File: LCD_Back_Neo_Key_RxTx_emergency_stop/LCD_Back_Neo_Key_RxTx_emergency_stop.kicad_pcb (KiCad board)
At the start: 2 copper layers, 109.7 x 102.1 mm, 27 parts, among them J1 Screw_Terminal_01x14, J2 Conn_01x20_Female, J3 Conn_01x08_Male_KeyPad, J4 Display_support_pin, J5 Display_support_pin, K1 FINDER-34.51, K2 FINDER-34.51, K3 FINDER-34.51, K4 FINDER-34.51, Q1 BC337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

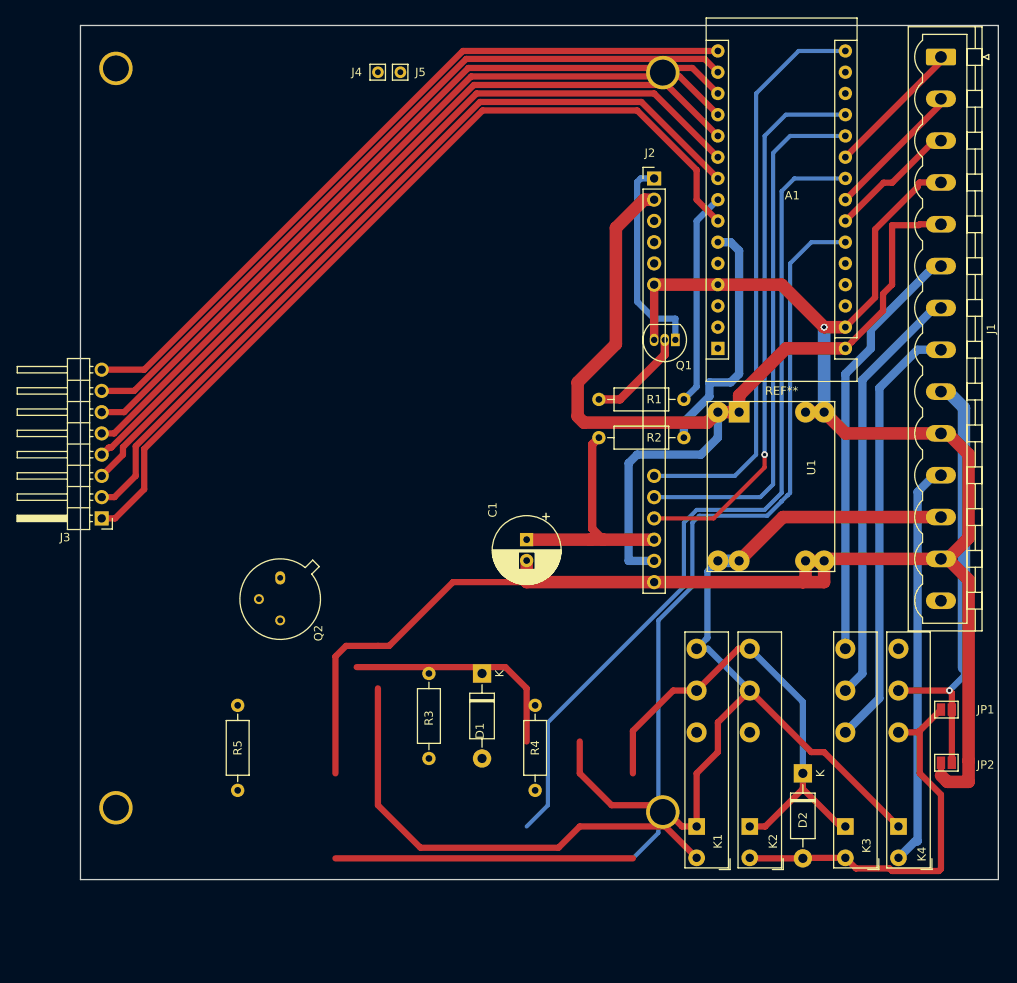
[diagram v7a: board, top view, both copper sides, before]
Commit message: make mounting holes free from tracks
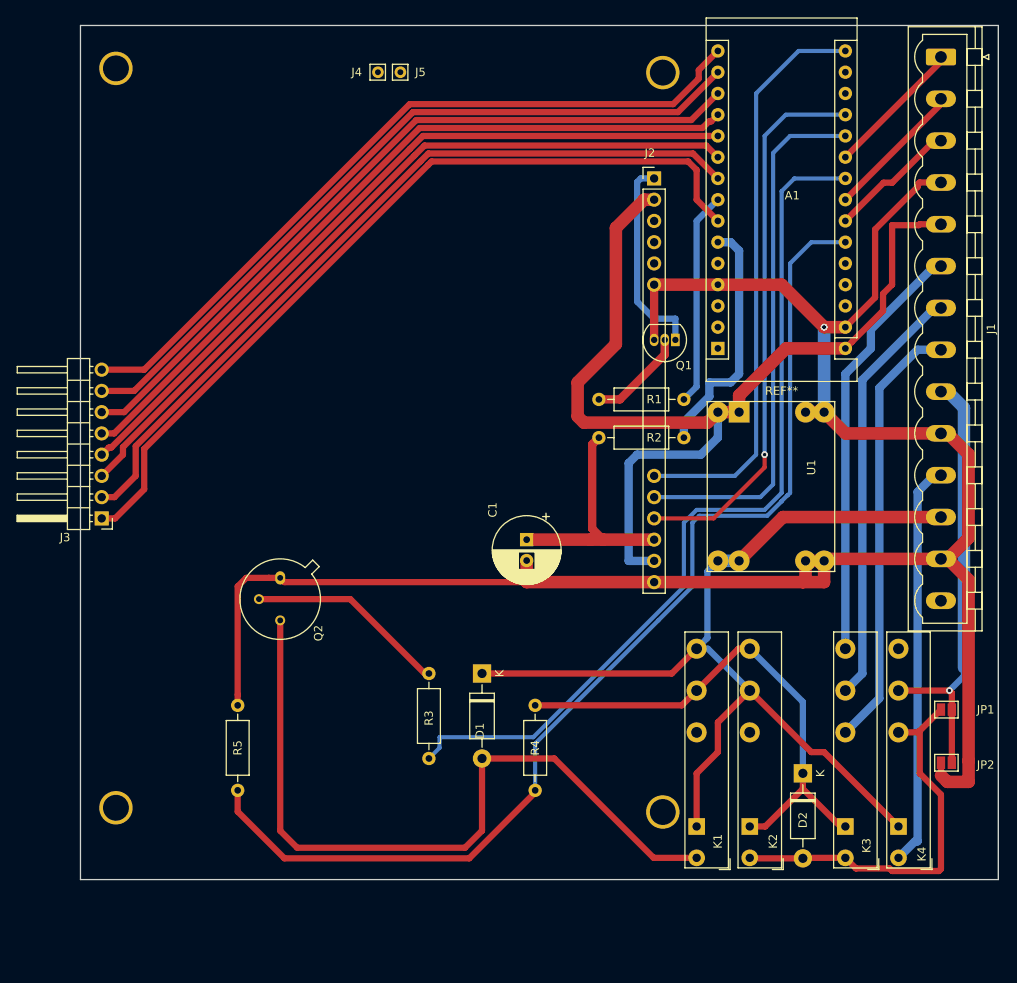
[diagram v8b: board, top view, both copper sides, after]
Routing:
- net Net-(D1-Pad2): track 56.8 -> 90.2 mm
- net GND: track 234.2 -> 243.0 mm
- net VCC-24V: track 112.6 -> 119.1 mm
- net Net-(D2-Pad1): track 57.7 -> 63.0 mm
- net Ardu_D7: track 96.3 -> 91.1 mm
- net Ardu_D6: track 99.1 -> 94.0 mm
- net Ardu_A6: track 126.9 -> 132.0 mm
- net Ardu_D8: track 94.5 -> 89.4 mm
- net Ardu_D4: track 104.2 -> 99.2 mm
- net Ardu_D9: track 93.2 -> 89.4 mm
- net Net-(Q2-Pad2): track 27.7 -> 24.0 mm
- net Ardu_A3: track 101.6 -> 104.9 mm
- net Ardu_D10: track 92.0 -> 89.4 mm
- net Ardu_D11: track 90.8 -> 89.4 mm
- net Ardu_D12: track 89.4 -> 90.0 mm
